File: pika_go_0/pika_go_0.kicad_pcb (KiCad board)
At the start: 4 copper layers, 50 x 110 mm, 113 parts, among them J1 USB_C_Receptacle_USB2.0_16P, J3 MCU_DEBUG, J4 SD_CARD, J5 Conn_01x02, J6 LCD, J7 MIC, J8 SPK, J9 ANT, Q1 BSS138, SW1 LSN, SW2 PTT, SW3 UP, SW4 DOWN, SW5 LEFT, SW6 RIGHT, SW7 PWR, U1 TLV75533PDBV, U10 TPS542025DDCR, U2 BQ25887RGE, U3 STM32H733VGTx, U4 SSM2305RMZ-REEL7, U5 MAX4467EKA_T, U6 E22-900M30S, U7 CAM-M8Q-0, U8 USB3300-EZK, U9 MCP1703Ax-330xxMB, Y1 SG-210STF 24.0000ML0

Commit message: Libraries cleanup, schematics finished, copper tracing finished, still need some PCB cleanup
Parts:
- removed C1, C2, C8: 10u, Capacitor_SMD:C_1210_3225Metric_Pad1.33x2.70mm_HandSolder
- removed C21, C47, C48, C50: 100n, Capacitor_SMD:C_0603_1608Metric_Pad1.08x0.95mm_HandSolder
- removed C51, C52: 22u, Capacitor_SMD:C_1210_3225Metric_Pad1.33x2.70mm_HandSolder
- removed FB1: 2508056017Y2, Inductor_SMD:L_0805_2012Metric_Pad1.05x1.20mm_HandSolder
- removed L1: 1u, Inductor_SMD:L_1210_3225Metric_Pad1.42x2.65mm_HandSolder
- removed L2: 10u, ton_library:IND_SRP4021HMCT-100M
- removed RN1: 10k, Resistor_SMD:R_Array_Convex_4x0603
- removed TH1: 10k, Connector_Wire:SolderWire-0.15sqmm_1x02_P4mm_D0.5mm_OD1.5mm
- removed U10: TPS542025DDCR, Package_TO_SOT_SMD:SOT-23-6
- removed U2: BQ25887RGE, Package_DFN_QFN:Texas_RGE0024H_VQFN-24-1EP_4x4mm_P0.5mm_EP2.7x2.7mm
- added C61: 22u, Capacitor_SMD:C_1210_3225Metric_Pad1.33x2.70mm_HandSolder, F.Cu at (59.1, 133.3)
- added C64: 100n, Capacitor_SMD:C_0603_1608Metric_Pad1.08x0.95mm_HandSolder, F.Cu at (59.9, 130.9)
- added C69: 4.7u, Capacitor_SMD:C_0603_1608Metric_Pad1.08x0.95mm_HandSolder, F.Cu at (70.5, 122.2)
- added C70: 22u, Capacitor_SMD:C_1210_3225Metric_Pad1.33x2.70mm_HandSolder, F.Cu at (69.8, 132.7)
- added C71: 22u, Capacitor_SMD:C_1210_3225Metric_Pad1.33x2.70mm_HandSolder, F.Cu at (73.0, 132.7)
- added C72: 100n, Capacitor_SMD:C_0603_1608Metric_Pad1.08x0.95mm_HandSolder, F.Cu at (67.4, 132.1)
- added D2: BAT54WS, Diode_SMD:D_SOD-323_HandSoldering, B.Cu at (50.9, 98.0)
- added FB4: 2508056017Y2, Inductor_SMD:L_0805_2012Metric_Pad1.05x1.20mm_HandSolder, B.Cu at (60.4, 100.8)
- added J2: BAT, Connector_JST:JST_PH_S3B-PH-K_1x03_P2.00mm_Horizontal, B.Cu at (38.5, 136.0)
- added L3: 2.2u, Inductor_SMD:L_1210_3225Metric_Pad1.42x2.65mm_HandSolder, F.Cu at (37.5, 130.2)
- added L6: 1u, Pika:L_ABRACON_AMELH4018S, F.Cu at (62.5, 127.4)
- added R27: 10k, Resistor_SMD:R_0603_1608Metric_Pad0.98x0.95mm_HandSolder, F.Cu at (47.1, 126.6)
- added R31: 0, Resistor_SMD:R_0603_1608Metric_Pad0.98x0.95mm_HandSolder, F.Cu at (64.0, 135.5)
- added U11: TPS610333DRLR, Package_TO_SOT_SMD:SOT-583-8, F.Cu at (64.0, 132.4)
- added U13: BQ25895RTW, Package_DFN_QFN:Texas_RTW_WQFN-24-1EP_4x4mm_P0.5mm_EP2.7x2.7mm_ThermalVias, F.Cu at (41.0, 124.7)
- C3, C4, C9, D1, R1: moved to F.Cu
- C36: value 100n -> 47n; moved to F.Cu
- C46: value 10u -> 100n; footprint Capacitor_SMD:C_1210_3225Metric_Pad1.33x2.70mm_HandSolder -> Capacitor_SMD:C_0603_1608Metric_Pad1.08x0.95mm_HandSolder; moved to B.Cu
- C6: value 47n -> 10u; footprint Capacitor_SMD:C_0603_1608Metric_Pad1.08x0.95mm_HandSolder -> Capacitor_SMD:C_1210_3225Metric_Pad1.33x2.70mm_HandSolder; moved to F.Cu
- FB2: moved to B.Cu
- J1: footprint ton_library:AMPHENOL_12402484E512A -> Pika:AMPHENOL_12402484E512A; moved to F.Cu
- J4: value SD_CARD -> Micro_SD_Card_Det1; footprint ton_library:503182-1852_MOL -> Pika:CUI_MSD-1-A
- J6: footprint ton_library:527461471_MOL -> Pika:527461471_MOL
- R2: value 383 -> 260
- R5, R6: value 47 -> 10k; footprint Resistor_SMD:R_1225_3264Metric_Pad1.47x6.45mm_HandSolder -> Resistor_SMD:R_0603_1608Metric_Pad0.98x0.95mm_HandSolder
- R9: value 300 -> 10k; moved to F.Cu
- SW3, SW4, SW5, SW6: footprint ton_library:TE_STSA -> Pika:TE_STSA
- U1: value TLV75533PDBV -> MCP1703Ax-500xxTT; footprint Package_TO_SOT_SMD:SOT-23-5 -> Package_TO_SOT_SMD:SOT-23
- U6: footprint ton_library:XCVR_E22-900M30S -> Pika:XCVR_E22-900M30S
- U7: footprint ton_library:LCC100P960X1400X210-31N -> Pika:LCC100P960X1400X210-31N
- moved U1 23.6 mm to (50.9, 133.4), turned to 180 degrees
- moved C46 21.5 mm to (62.5, 124.8), turned to 90 degrees
- moved C5 18.9 mm to (45.6, 126.6), turned to -90 degrees
- moved C3 15.3 mm to (34.4, 123.8), turned to 0 degrees
- moved R2 14.7 mm to (47.5, 130.2), turned to -90 degrees
- moved R4 14.2 mm to (46.0, 133.5), turned to -90 degrees
- moved C45 14.1 mm to (54.0, 133.3), turned to -90 degrees
- moved NT1 13.9 mm to (46.3, 130.6), turned to 90 degrees
- moved J4 13.0 mm to (72.8, 127.0)
- moved C9 11.7 mm to (34.4, 120.7), turned to 180 degrees
- moved FB2 11.0 mm to (59.0, 131.0), turned to -90 degrees
- moved C4 10.9 mm to (34.4, 127.0), turned to 0 degrees
- moved R9 10.3 mm to (46.5, 123.9), turned to 180 degrees
- moved C7 9.82 mm to (43.3, 132.6), turned to 0 degrees
- moved R3 9.66 mm to (43.3, 134.1), turned to 180 degrees
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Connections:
- net /USB Power/USB_DM renamed /USB/USB_DM
- net /USB Power/USB_DP renamed /USB/USB_DP
- net /USB Power/USB_VDD1.8 renamed /USB/USB_VDD1.8
- net /USB Power/USB_VDDA1.8 renamed /USB/USB_VDDA1.8
- net /USB Power/USB_VDDA3.3 renamed /USB/USB_VDDA3.3
- net Net-(U2-REGN) renamed /Power/REGN
- net Net-(U2-TS) renamed /Power/TS
- C3 pad 2: VSYS -> /Power/SYS
- C36 pad 1: GNDA -> Net-(C36-Pad1)
- C36 pad 2: Net-(U2-MID) -> Net-(U13-BTST)
- C4 pad 2: VSYS -> /Power/SYS
- C41 pad 1: /USB Power/USB_VDD3.3 -> /USB/USB_VDD3.3
- C42 pad 1: /USB Power/USB_VDD3.3 -> /USB/USB_VDD3.3
- C45 pad 1: /USB Power/USB_VDD3.3 -> /USB/USB_VDD3.3
- C46 pad 1: /USB Power/BAT -> +3.3V
- C5 pad 1: /USB Power/USB_VBUS -> USB_VBUS
- C6 pad 1: Net-(C6-Pad1) -> GND
- C9 pad 1: /USB Power/BAT -> /Power/BAT
- FB2 pad 1: /USB Power/USB_VDD3.3 -> /USB/USB_VDD3.3
- J1 pad A4: /USB Power/USB_VBUS -> USB_VBUS
- J1 pad A9: /USB Power/USB_VBUS -> USB_VBUS
- J1 pad B4: /USB Power/USB_VBUS -> USB_VBUS
- J1 pad B9: /USB Power/USB_VBUS -> USB_VBUS
- J4 pad 9: (no net) -> unconnected-(J4-DET-Pad9)
- R1 pad 1: /USB Power/USB_VBUS -> /Power/SYS
- R5 pad 1: Net-(U2-CBSET) -> +3.3V
- R5 pad 2: Net-(J2-Pin_2) -> CHG_INT
- R6 pad 1: Net-(U2-CBSET) -> +3.3V
- R6 pad 2: Net-(J2-Pin_2) -> CHG_I2C_SDA
- R8 pad 2: /USB Power/USB_VBUS -> USB_VBUS
- R9 pad 1: Net-(J2-Pin_2) -> +3.3V
- R9 pad 2: Net-(U2-MID) -> CHG_I2C_SCL
- SW7 pad 1: /MCU/BTN_PWR -> BTN_PWR
- U1 pad 1: +5V -> GND
- U1 pad 2: GND -> /USB/USB_VDD3.3
- U1 pad 3: +5V -> USB_VBUS
- U3 pad 40: /MCU/BTN_PWR -> Net-(D2-A)
- U3 pad 95: CHG_PSEL -> unconnected-(U3-PB8-Pad95)
- U3 pad 96: CHG_CD -> unconnected-(U3-PB9-Pad96)
- U8 pad 16: /USB Power/USB_VDD3.3 -> /USB/USB_VDD3.3
- U8 pad 25: /USB Power/USB_VDD3.3 -> /USB/USB_VDD3.3
- U8 pad 31: /USB Power/USB_VDD3.3 -> /USB/USB_VDD3.3
- U9 pad 2: /USB Power/USB_VBUS -> +5V
- U9 pad 3: /USB Power/USB_VDD3.3 -> +3.3V
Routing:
- net BTN_PWR: track 0.00 -> 102.4 mm, vias 0 -> 2
- net /MCU/BTN_PWR: track 72.9 -> 0.00 mm, vias 2 -> 0
- net /USB Power/USB_VBUS: track 59.2 -> 0.00 mm, vias 3 -> 0
- net /Power/SYS: track 0.00 -> 43.9 mm
- net /USB Power/USB_VDD3.3: track 38.3 -> 0.00 mm, vias 3 -> 0
- net +3.3VA: track 98.8 -> 61.4 mm
- net /USB/USB_VDD3.3: track 0.00 -> 37.0 mm, vias 0 -> 3
- net CHG_PG: track 29.6 -> 0.00 mm
- net USB_VBUS: track 0.00 -> 26.5 mm
- net CHG_PSEL: track 23.3 -> 0.00 mm, vias 2 -> 0
- net CHG_CD: track 22.7 -> 0.00 mm, vias 2 -> 0
- net +5V: track 115.1 -> 93.0 mm, vias 4 -> 2
- net /Power/BAT: track 0.00 -> 16.6 mm, vias 0 -> 1
- net CHG_I2C_SCL: track 44.7 -> 28.6 mm, vias 2 -> 1
- net CHG_I2C_SDA: track 45.0 -> 31.3 mm, vias 2 -> 1
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
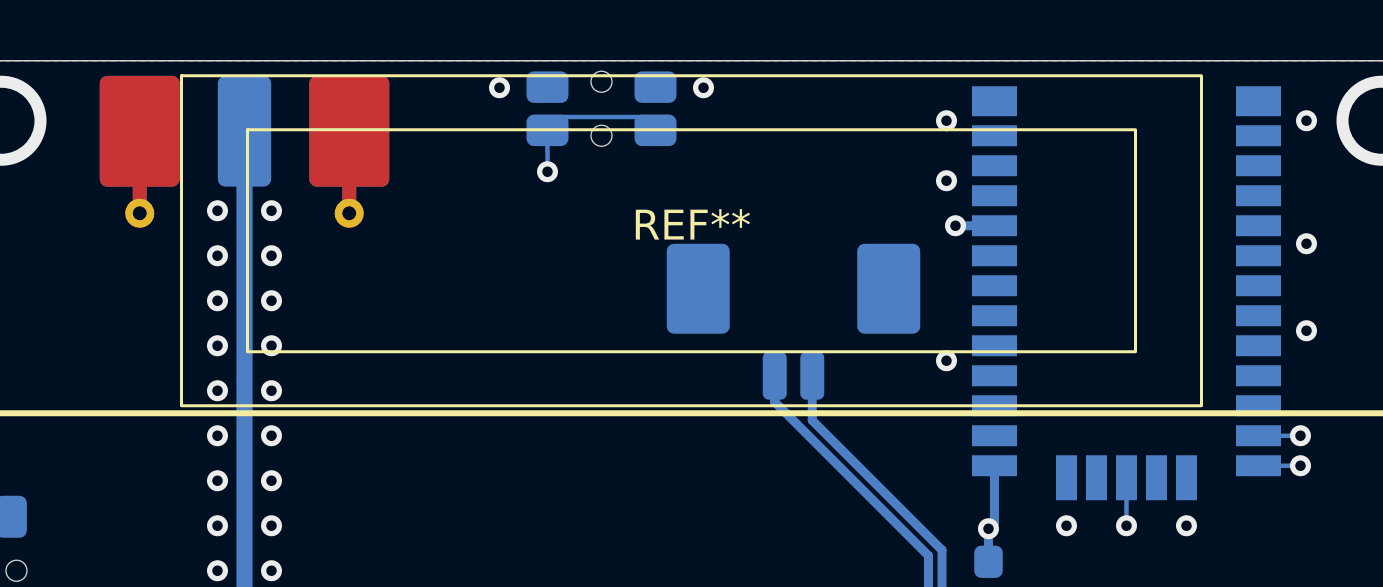
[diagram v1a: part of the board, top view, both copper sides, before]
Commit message: Footprint library fixes, missing 3D models added
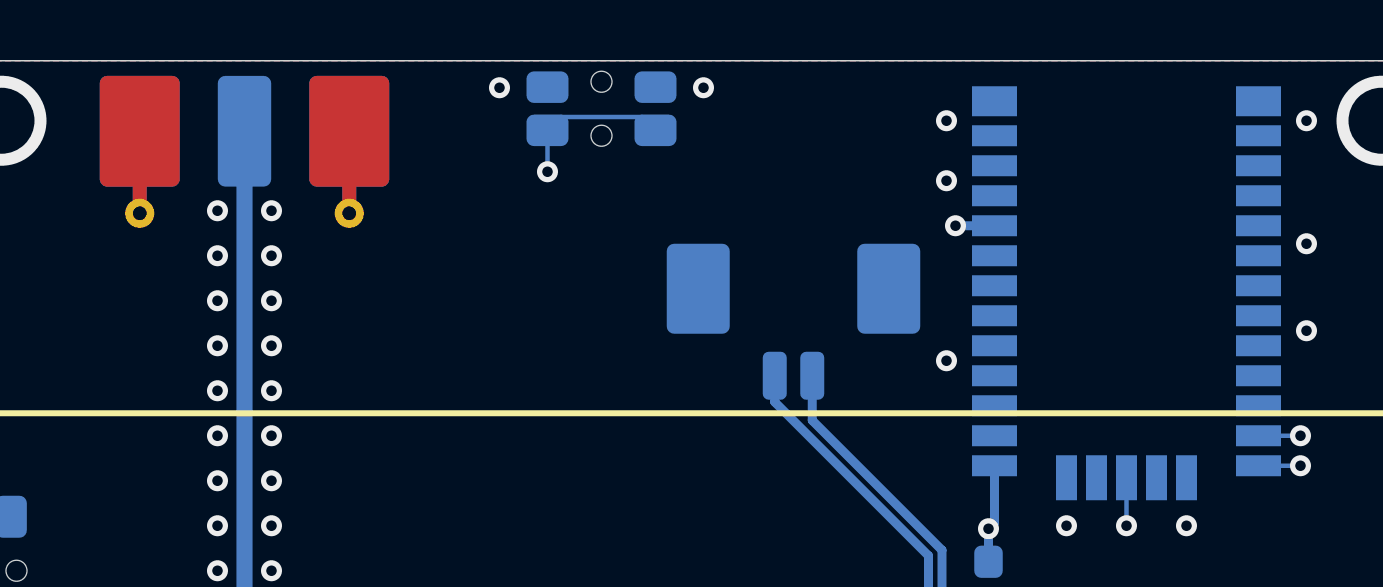
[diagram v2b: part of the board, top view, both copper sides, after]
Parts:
- removed REF**: OWS-113440TA-4, ton_library:OWS-113440TA-4

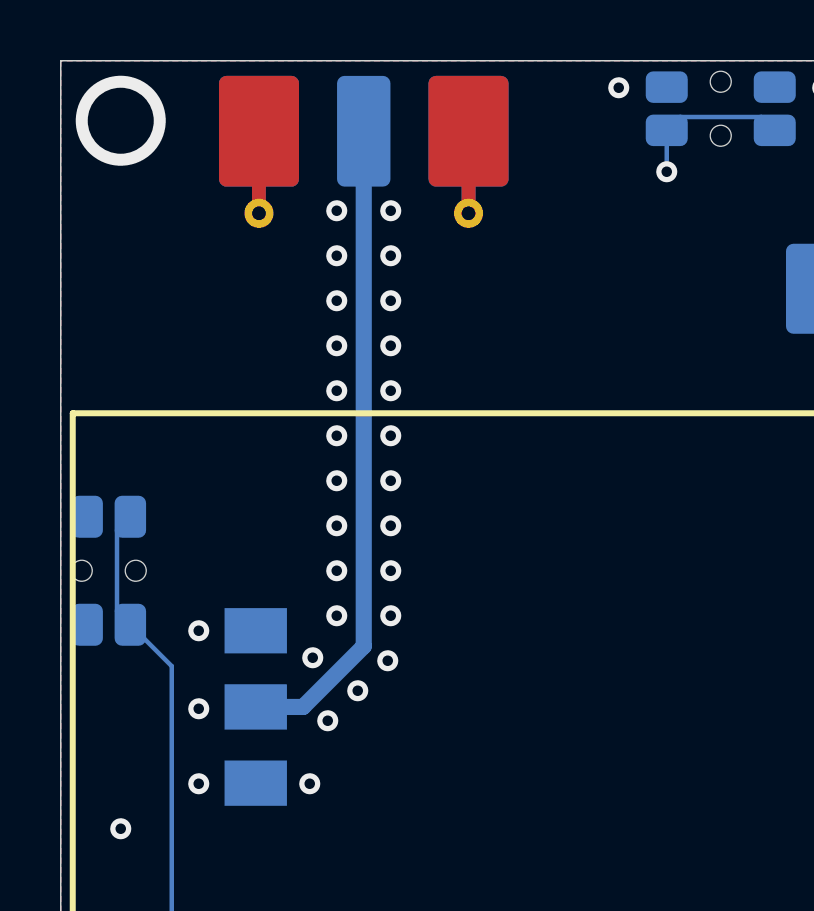
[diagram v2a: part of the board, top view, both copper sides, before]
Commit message: More 3D models added to library. Use external SMA-U.FL cable instead in SMA connector on PCB edge.
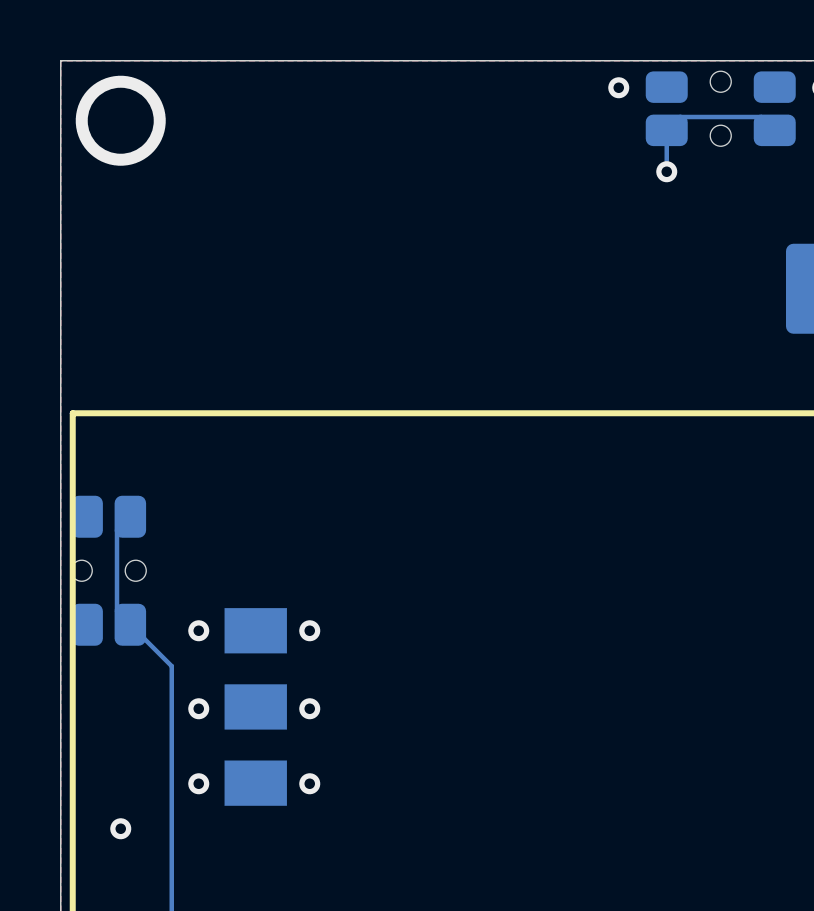
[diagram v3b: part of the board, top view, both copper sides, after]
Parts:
- removed J9: ANT, Connector_Coaxial:SMA_Molex_73251-2120_EdgeMount_Horizontal
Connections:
- U6 pad 21: /Radio/ANT -> unconnected-(U6-ANT-Pad21)
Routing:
- net /Radio/ANT: track 21.6 -> 0.00 mm
- net GND: vias 172 -> 150

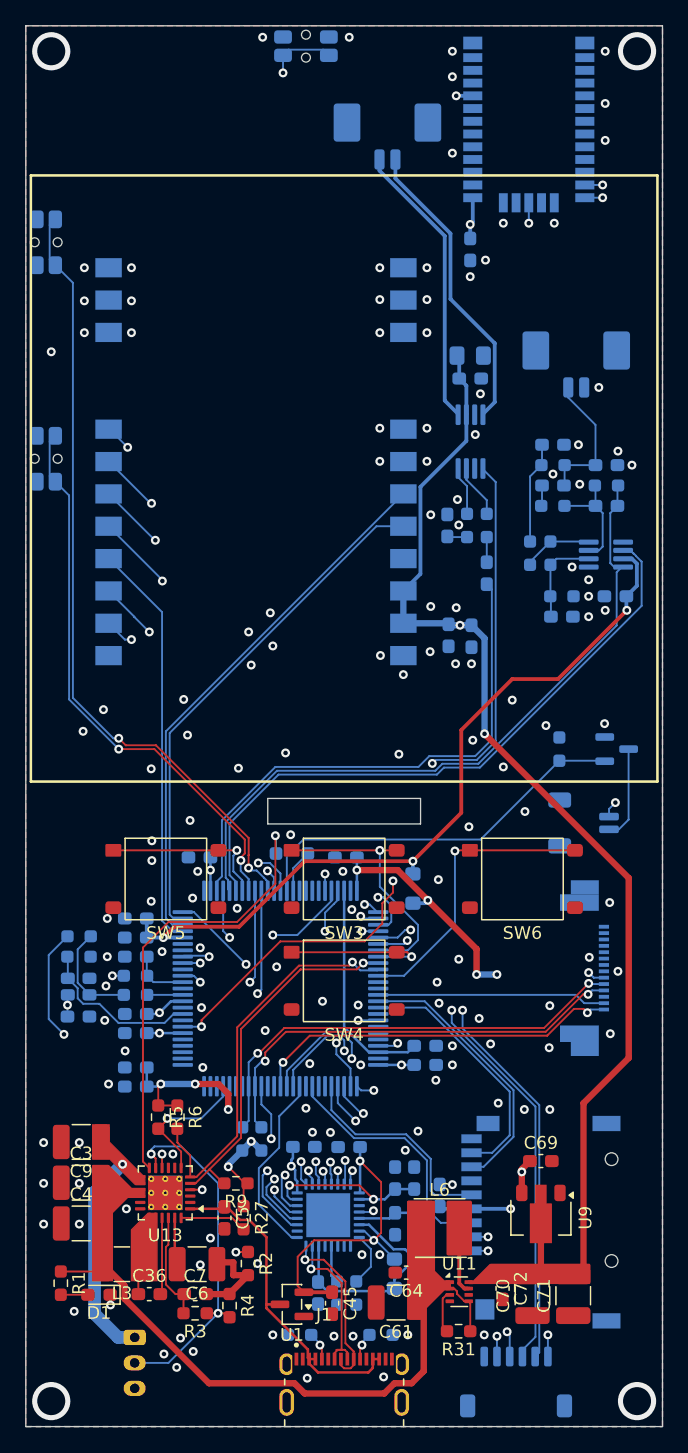
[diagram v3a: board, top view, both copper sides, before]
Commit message: Some capacitors footprints changed, minor cleanup
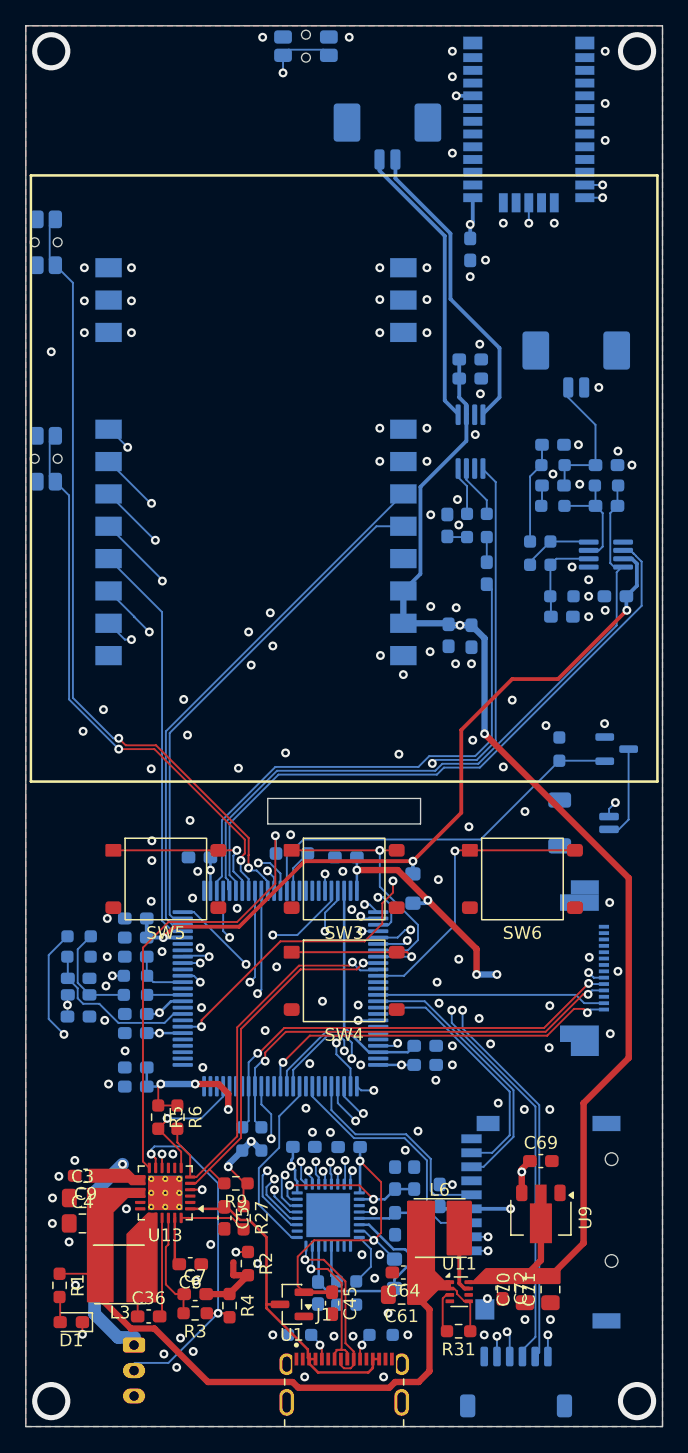
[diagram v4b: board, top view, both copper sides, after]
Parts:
- C3, C4, C61, C70, C71: footprint Capacitor_SMD:C_1210_3225Metric_Pad1.33x2.70mm_HandSolder -> Capacitor_SMD:C_0805_2012Metric_Pad1.18x1.45mm_HandSolder
- C31: footprint Capacitor_SMD:C_0805_2012Metric_Pad1.18x1.45mm_HandSolder -> Capacitor_SMD:C_0603_1608Metric_Pad1.08x0.95mm_HandSolder
- C6, C9: footprint Capacitor_SMD:C_1210_3225Metric_Pad1.33x2.70mm_HandSolder -> Capacitor_SMD:C_0603_1608Metric_Pad1.08x0.95mm_HandSolder
- L3: value 2.2u -> 1u; footprint Inductor_SMD:L_1210_3225Metric_Pad1.42x2.65mm_HandSolder -> Pika:L_ABRACON_AMELH4018S
- R2: value 260 -> 261
- moved D1 3.06 mm to (33.6, 134.8)
- moved C9 2.67 mm to (34.7, 123.3)
- moved C71 1.85 mm to (71.2, 132.2)
- moved C36 1.75 mm to (39.6, 134.3)
- moved C3 1.21 mm to (34.5, 125.0)
- moved L3 0.81 mm to (37.4, 131.1)
- moved C70 0.76 mm to (69.2, 132.2)
- moved C61 0.75 mm to (59.5, 132.7)
- moved J2 0.60 mm to (38.5, 136.6)
- moved C6 0.54 mm to (42.9, 130.2)
- moved C31 0.30 mm to (64.9, 59.2)
- moved C64 0.23 mm to (59.6, 130.9)
- moved R1 0.20 mm to (32.6, 131.9)
- moved C4 0.10 mm to (34.5, 127.0)
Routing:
- net Net-(D1-K): track 13.9 -> 17.2 mm
- net Net-(U13-BTST): track 5.85 -> 7.82 mm
- net /Power/SYS: track 43.9 -> 45.3 mm
- net Net-(C36-Pad1): track 2.15 -> 3.37 mm
- net GND: track 1.14 -> 0.00 mm, vias 150 -> 155
- net +5V: track 93.0 -> 94.0 mm

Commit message: Schematic reannotated, cleanup
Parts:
- removed U13: BQ25895RTW, Package_DFN_QFN:Texas_RTW_WQFN-24-1EP_4x4mm_P0.5mm_EP2.7x2.7mm_ThermalVias
- added U2: BQ25895RTW, Package_DFN_QFN:Texas_RTW_WQFN-24-1EP_4x4mm_P0.5mm_EP2.7x2.7mm_ThermalVias, F.Cu at (41.0, 124.7)
- moved J4 2.30 mm to (71.5, 95.6)
- renumbered C61 to C1, C72 to C10, C7 to C11, C9 to C12, C69 to C13, C10 to C14, C35 to C15, C11 to C16, C12 to C17, C13 to C18, C14 to C19, C64 to C2, C15 to C20, C16 to C21, C17 to C22, C18 to C23, C19 to C24, C20 to C25, C46 to C26, C41 to C27, C42 to C28, C44 to C29, C5 to C3, C43 to C30, C37 to C31, C38 to C32, C45 to C33, C39 to C34, C40 to C35, C32 to C36, C33 to C37, C34 to C38, C22 to C39, C36 to C4, C23 to C40, C24 to C41, C25 to C42, C26 to C43, C27 to C44, C28 to C45, C29 to C46, C30 to C47, C31 to C48, C3 to C5, C4 to C7, C70 to C8, C71 to C9, FB4 to FB1, J2 to J1, J3 to J2, J4 to J3, J5 to J4, J6 to J5, J1 to J6, L6 to L1, L3 to L2, R5 to R1, R22 to R10, R26 to R11, R25 to R12, R10 to R13, R12 to R14, R11 to R15, R13 to R16, R8 to R17, R7 to R18, R23 to R19, R6 to R2, R24 to R20, R14 to R21, R15 to R22, R16 to R23, R17 to R24, R18 to R25, R19 to R26, R20 to R27, R21 to R28, R9 to R3, R2 to R4, R31 to R5, R27 to R6, R1 to R7, R3 to R8, R4 to R9, SW7 to SW1, SW1 to SW2, SW2 to SW3, SW3 to SW4, SW4 to SW5, SW5 to SW6, SW6 to SW7, U11 to U1, U5 to U10, U9 to U3, U3 to U4, U8 to U5, U1 to U6, U6 to U7, U7 to U8, U4 to U9
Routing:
- net USB_VBUS: track 26.5 -> 32.2 mm, vias 0 -> 1
- net Net-(J4-Pin_1): track 7.39 -> 8.59 mm
- net /Power/BAT: track 16.6 -> 15.7 mm
- net GND: vias 155 -> 157
